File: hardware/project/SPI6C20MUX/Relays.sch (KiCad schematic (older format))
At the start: 82 parts, among them J201 5499141-4, K201 HE3621A0510, K202 HE3621A0510, K203 HE3621A0510, K204 HE3621A0510, K205 HE3621A0510, K206 HE3621A0510, K207 HE3621A0510, K208 HE3621A0510, K209 HE3621A0510, K210 HE3621A0510, K211 HE3621A0510, K212 HE3621A0510, K213 HE3621A0510, K214 HE3621A0510, K215 HE3621A0510, K216 HE3621A0510, K217 HE3621A0510, K218 HE3621A0510, K219 HE3621A0510, K220 HE3621A0510, K221 HE3621A0510, K222 HE3621A0510, K223 HE3621A0510, K224 HE3621A0510, K225 HE3621A0510, K226 HE3621A0510, K227 HE3621A0510, K228 HE3621A0510, K229 HE3621A0510, K230 HE3621A0510, K231 HE3621A0510, K232 HE3621A0510, K233 HE3621A0510, K234 HE3621A0510, K235 HE3621A0510, K236 HE3621A0510, K237 HE3621A0510, K238 HE3621A0510, K239 HE3621A0510, K240 HE3621A0510, K241 HE3621A0510, K242 HE3621A0510, K243 HE3621A0510, K244 HE3621A0510, K245 HE3621A0510, K246 HE3621A0510, K247 HE3621A0510, K248 HE3621A0510, K249 HE3621A0510, K250 HE3621A0510, K251 HE3621A0510, K252 HE3621A0510, K253 HE3621A0510, K254 HE3621A0510, K255 HE3621A0510, K256 HE3621A0510, K257 HE3621A0510, K258 HE3621A0510, K259 HE3621A0510, K260 HE3621A0510, K261 HE3621A0510, K262 HE3621A0510, K263 HE3621A0510, K264 HE3621A0510, K265 HE3621A0510, K266 HE3621A0510, U201 MCZ33996, U202 MCZ33996, U203 MCZ33996, U204 MCZ33996, U205 MCZ33996

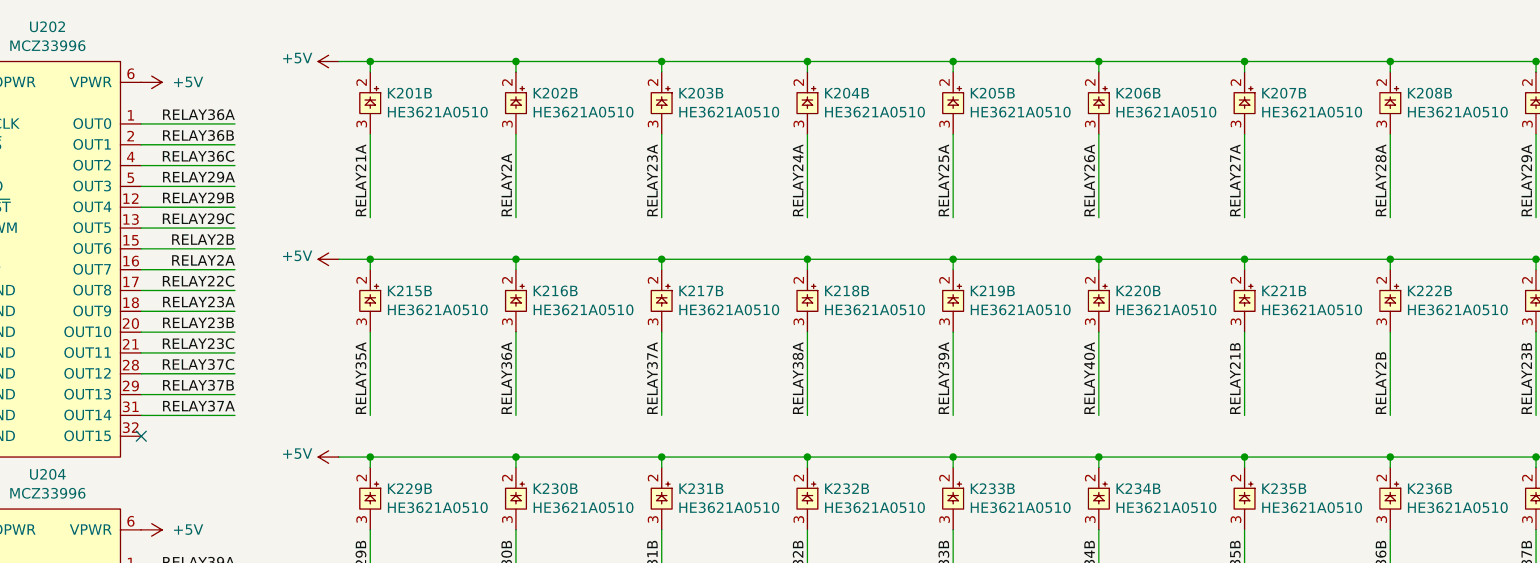
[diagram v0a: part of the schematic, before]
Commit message: SPI6C20MUX layout done, bug fixes in ETH6C20MUX layout.
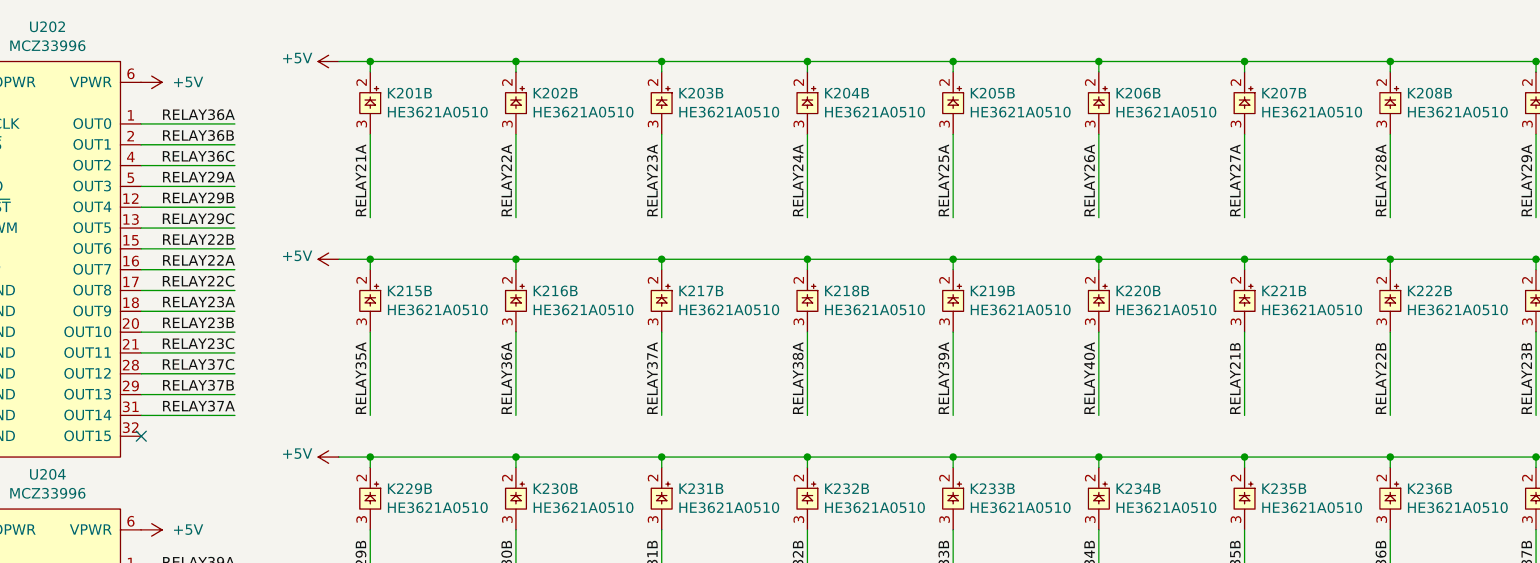
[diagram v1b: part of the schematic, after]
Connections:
- net RELAY2A renamed RELAY22A
- net RELAY2B renamed RELAY22B
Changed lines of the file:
@@
 RELAY21A
 Text Label 6800 1500 1    50   ~ 0
-RELAY2A
+RELAY22A
 Text Label 8200 1500 1    50   ~ 0
 RELAY24A
@@
 RELAY21B
 Text Label 11000 2450 1    50   ~ 0
-RELAY2B
+RELAY22B
 Text Label 11700 2450 1    50   ~ 0
 RELAY23B
@@
 RELAY23B
 Text Label 5450 1650 2    50   ~ 0
-RELAY2B
+RELAY22B
 Text Label 3150 1750 2    50   ~ 0
 RELAY21B
@@
 RELAY23A
 Text Label 5450 1750 2    50   ~ 0
-RELAY2A
+RELAY22A
 Text Label 3150 1050 2    50   ~ 0
 RELAY21A

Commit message: PCB main and module layout.
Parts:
- added K267, K268, K269, K270: HE3621A0510, ETH6C20MUX:HE360_x-5331272-5, symbol ETH6C20MUX:HE3621A0510
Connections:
- net +5V: now also K267.2, K268.2, K269.2, K270.2
- net A: now also K269.1
- net B: now also K267.1
- net E: now also K268.1
- net F: now also K270.1
- net PIN21A: now also K267.4, K268.4
- net PIN21B: now also K269.4, K270.4
- net RELAY21A: now also U201.16 (OUT7); no longer U201.1 (OUT0)
- net RELAY21B: now also U201.1 (OUT0); no longer U201.16 (OUT7)
- net RELAY21C: now also U201.28 (OUT12); no longer U201.17 (OUT8)
- net RELAY22A: now also U201.32 (OUT15); no longer U202.16 (OUT7)
- net RELAY22B: now also U202.1 (OUT0); no longer U202.15 (OUT6)
- net RELAY22C: now also U202.21 (OUT11); no longer U202.17 (OUT8)
- net RELAY23A: now also U203.1 (OUT0); no longer U202.18 (OUT9)
- net RELAY23B: now also U203.2 (OUT1); no longer U202.20 (OUT10)
- net RELAY23C: now also U203.16 (OUT7); no longer U202.21 (OUT11)
- net RELAY24A: now also U203.32 (OUT15); no longer U203.4 (OUT2)
- net RELAY24B: now also U203.31 (OUT14); no longer U203.2 (OUT1)
- net RELAY24C: now also U203.29 (OUT13); no longer U203.1 (OUT0)
- net RELAY25A: now also U204.1 (OUT0); no longer U203.31 (OUT14)
- net RELAY25B: now also U204.2 (OUT1); no longer U203.29 (OUT13)
- net RELAY25C: now also U204.17 (OUT8); no longer U203.28 (OUT12)
- net RELAY26A: now also U204.18 (OUT9); no longer U204.28 (OUT12)
- net RELAY26B: now also U204.20 (OUT10); no longer U204.29 (OUT13)
- net RELAY26C: now also U204.21 (OUT11); no longer U204.31 (OUT14)
- net RELAY27A: now also U201.15 (OUT6); no longer U201.2 (OUT1)
- net RELAY27B: now also U201.2 (OUT1); no longer U201.13 (OUT5)
- net RELAY27C: now also U201.29 (OUT13); no longer U201.15 (OUT6)
- net RELAY28A: now also U202.2 (OUT1); no longer U201.28 (OUT12)
- net RELAY28B: now also U202.13 (OUT5); no longer U201.29 (OUT13)
- net RELAY28C: now also U202.12 (OUT4); no longer U201.31 (OUT14)
- net RELAY29A: now also U202.16 (OUT7); no longer U202.5 (OUT3)
- net RELAY29B: now also U202.15 (OUT6); no longer U202.12 (OUT4)
- net RELAY29C: now also U203.17 (OUT8); no longer U202.13 (OUT5)
- net RELAY30A: now also U203.28 (OUT12); no longer U203.13 (OUT5)
- net RELAY30B: now also U203.21 (OUT11); no longer U203.12 (OUT4)
- net RELAY30C: now also U203.20 (OUT10); no longer U203.5 (OUT3)
- net RELAY31B: now also U204.15 (OUT6); no longer U203.20 (OUT10)
- net RELAY31C: now also U204.13 (OUT5); no longer U203.21 (OUT11)
- net RELAY32A: now also U204.12 (OUT4); no longer U204.18 (OUT9)
- net RELAY32B: now also U204.5 (OUT3); no longer U204.20 (OUT10)
- net RELAY32C: now also U204.4 (OUT2); no longer U204.21 (OUT11)
- net RELAY33A: now also U205.17 (OUT8); no longer U205.5 (OUT3)
- net RELAY33B: now also U205.15 (OUT6); no longer U205.12 (OUT4)
- net RELAY34A: now also U205.16 (OUT7); no longer U201.4 (OUT2)
- net RELAY34B: now also U205.29 (OUT13); no longer U201.5 (OUT3)
- net RELAY34C: now also U205.31 (OUT14); no longer U201.12 (OUT4)
- net RELAY35A: now also U204.31 (OUT14); no longer U201.18 (OUT9)
- net RELAY35B: now also U204.32 (OUT15); no longer U201.20 (OUT10)
- net RELAY35C: now also U204.16 (OUT7); no longer U201.21 (OUT11)
- net RELAY36A: now also U203.4 (OUT2); no longer U202.1 (OUT0)
- net RELAY36B: now also U204.28 (OUT12); no longer U202.2 (OUT1)
- net RELAY36C: now also U204.29 (OUT13); no longer U202.4 (OUT2)
- net RELAY37A: now also U203.13 (OUT5); no longer U202.31 (OUT14)
- net RELAY37B: now also U203.12 (OUT4); no longer U202.29 (OUT13)
- net RELAY37C: now also U203.5 (OUT3); no longer U202.28 (OUT12)
- net RELAY38A: now also U202.32 (OUT15); no longer U203.15 (OUT6)
- net RELAY38B: now also U202.31 (OUT14); no longer U203.16 (OUT7)
- net RELAY38C: now also U203.15 (OUT6); no longer U203.17 (OUT8)
- net RELAY39A: now also U202.4 (OUT2); no longer U204.1 (OUT0)
- net RELAY39B: now also U202.29 (OUT13); no longer U204.2 (OUT1)
- net RELAY39C: now also U202.28 (OUT12); no longer U204.4 (OUT2)
- net RELAY40A: now also U201.13 (OUT5); no longer U205.1 (OUT0)
- net RELAY40B: now also U201.4 (OUT2); no longer U205.2 (OUT1)
- net RELAY40C: now also U201.31 (OUT14); no longer U205.4 (OUT2)
- net RELAYA: now also U205.21 (OUT11); no longer U205.31 (OUT14)
- net RELAYB: now also U205.28 (OUT12); no longer U205.29 (OUT13)
- net RELAYC: now also U205.32 (OUT15); no longer U205.28 (OUT12)
- net RELAYD: now also U205.12 (OUT4); no longer U205.21 (OUT11)
- net RELAYE: now also U205.5 (OUT3); no longer U205.20 (OUT10)
- net RELAYF: now also U205.4 (OUT2); no longer U205.18 (OUT9)
- new net RELAYAB: K269.3, U205.20 (OUT10)
- new net RELAYBA: K267.3, U205.1 (OUT0)
- new net RELAYEA: K268.3, U205.18 (OUT9)
- new net RELAYFA: K270.3, U205.2 (OUT1)
- no-connect marks 19 -> 15
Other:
- moved on the sheet: J201, K262A, K263A, K264A, K265A
